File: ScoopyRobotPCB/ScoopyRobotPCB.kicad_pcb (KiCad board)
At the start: 2 copper layers, 35 parts, among them J1 18V battery, J2 Raspberry_Pi_Header, J3 Left colour sensor, J4 Right colour sensor, J5 Wheels, J6 Power, J7 Left, J8 Right, M1 Chain gearmotor, M2 Left motor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

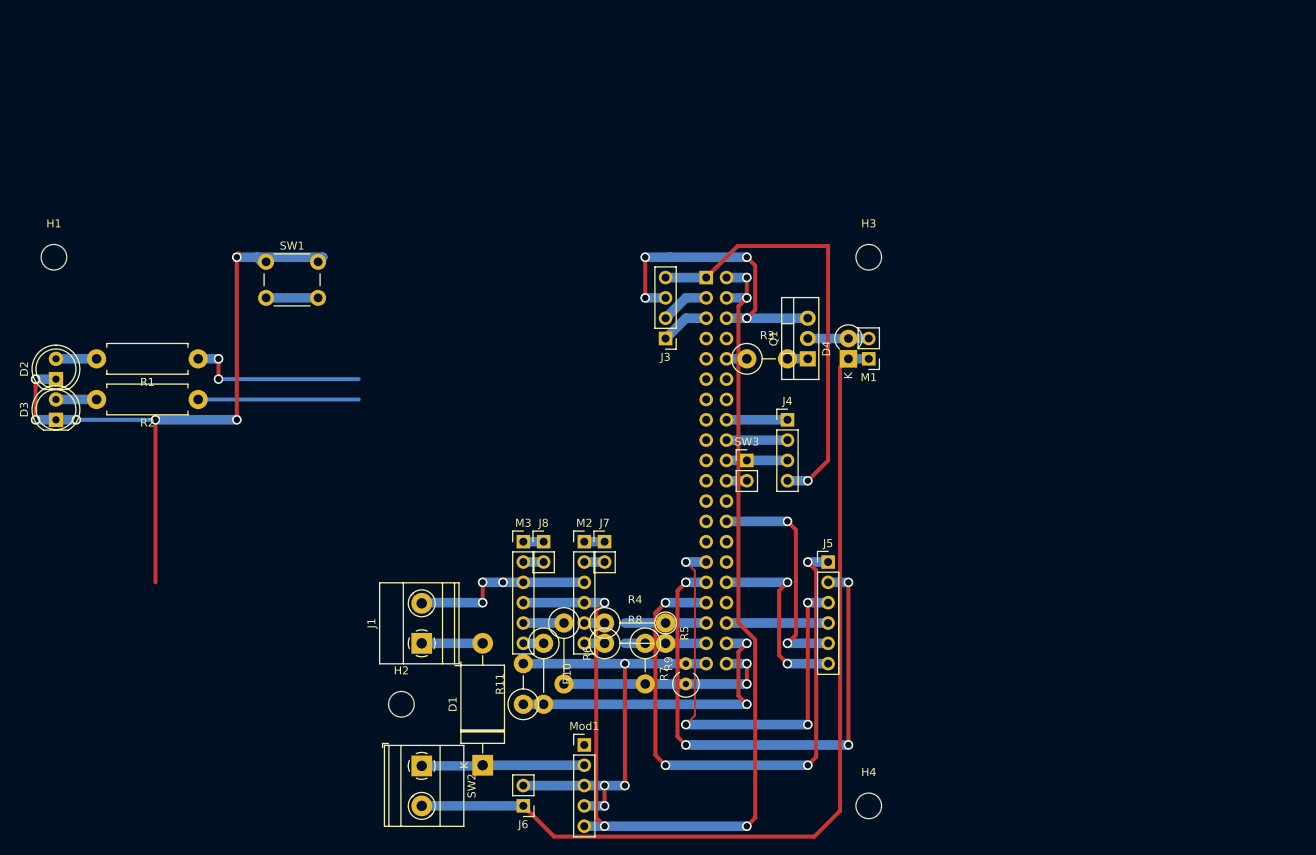
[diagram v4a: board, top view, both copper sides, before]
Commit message: Updated the PCB files to match reality
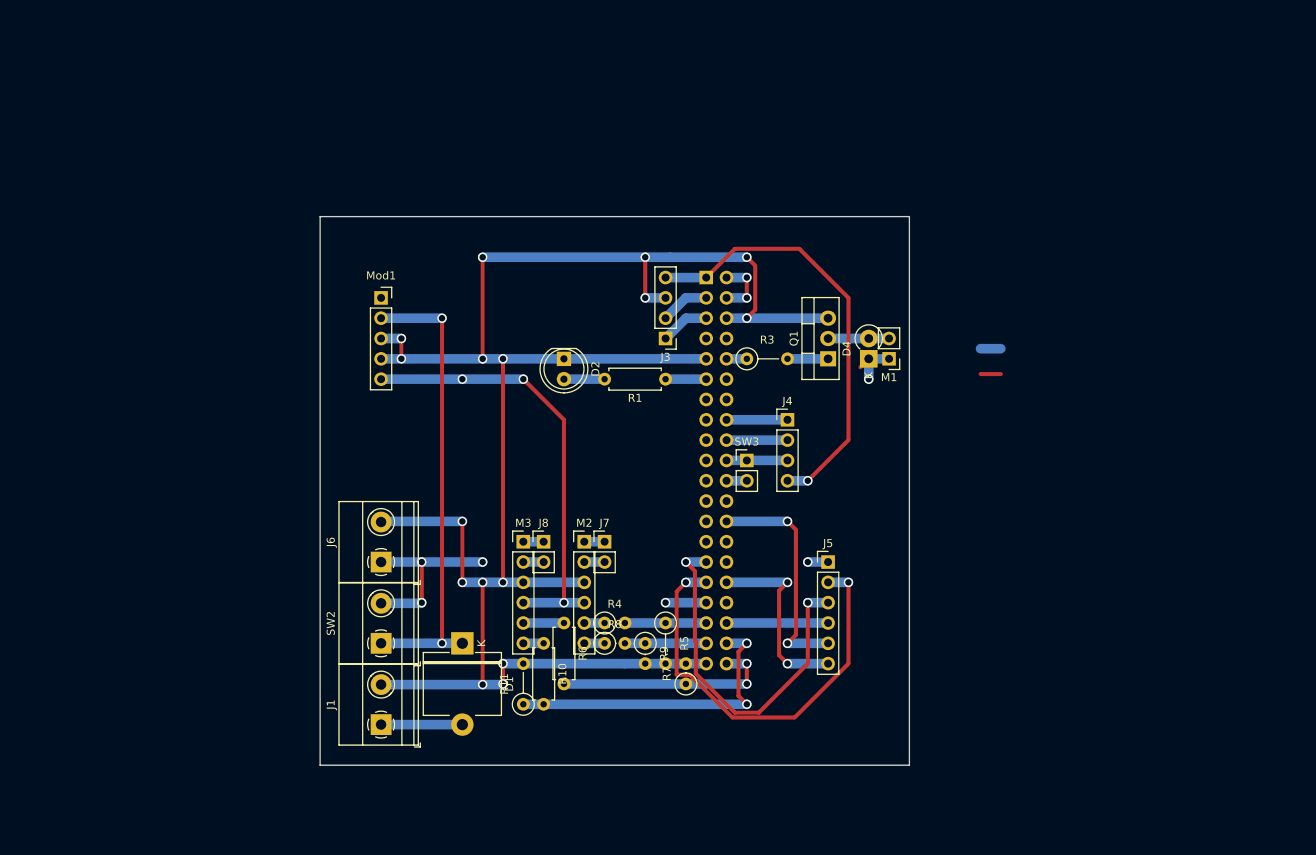
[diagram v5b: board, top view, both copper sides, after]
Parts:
- removed D3: LED, LED_THT:LED_D5.0mm
- removed H1, H2, H3, H4: MountingHole, MountingHole:MountingHole_3.2mm_M3
- removed R2: 220, Resistor_THT:R_Axial_DIN0411_L9.9mm_D3.6mm_P12.70mm_Horizontal
- removed SW1: SW_Push, Button_Switch_THT:SW_PUSH_6mm
- D1: footprint Diode_THT:D_DO-201_P15.24mm_Horizontal -> Diode_THT:D_5KP_P10.16mm_Horizontal
- J6: footprint Connector_PinHeader_2.54mm:PinHeader_1x02_P2.54mm_Vertical -> TerminalBlock_Phoenix:TerminalBlock_Phoenix_MKDS-1,5-2_1x02_P5.00mm_Horizontal
- Mod1: footprint Connector_PinHeader_2.54mm:PinHeader_1x05_P2.54mm_Vertical -> Connector_PinSocket_2.54mm:PinSocket_1x05_P2.54mm_Vertical
- Q1: value Q_NPN_Darlington_BCE -> 2SD1308
- R1: value 220 -> 150; footprint Resistor_THT:R_Axial_DIN0411_L9.9mm_D3.6mm_P12.70mm_Horizontal -> Resistor_THT:R_Axial_DIN0207_L6.3mm_D2.5mm_P7.62mm_Horizontal
- R10, R6: footprint Resistor_THT:R_Axial_DIN0411_L9.9mm_D3.6mm_P7.62mm_Vertical -> Resistor_THT:R_Axial_DIN0207_L6.3mm_D2.5mm_P7.62mm_Horizontal
- R11, R3: footprint Resistor_THT:R_Axial_DIN0411_L9.9mm_D3.6mm_P5.08mm_Vertical -> Resistor_THT:R_Axial_DIN0207_L6.3mm_D2.5mm_P5.08mm_Vertical
- R4, R8: footprint Resistor_THT:R_Axial_DIN0411_L9.9mm_D3.6mm_P7.62mm_Vertical -> Resistor_THT:R_Axial_DIN0207_L6.3mm_D2.5mm_P2.54mm_Vertical
- R5: footprint Resistor_THT:R_Axial_DIN0207_L6.3mm_D2.5mm_P2.54mm_Vertical -> Resistor_THT:R_Axial_DIN0207_L6.3mm_D2.5mm_P5.08mm_Vertical
- R7: footprint Resistor_THT:R_Axial_DIN0309_L9.0mm_D3.2mm_P2.54mm_Vertical -> Resistor_THT:R_Axial_DIN0207_L6.3mm_D2.5mm_P2.54mm_Vertical
- R9: footprint Resistor_THT:R_Axial_DIN0411_L9.9mm_D3.6mm_P5.08mm_Vertical -> Resistor_THT:R_Axial_DIN0207_L6.3mm_D2.5mm_P2.54mm_Vertical
- moved D2 63.6 mm to (109.2, 88.9), turned to -90 degrees
- moved Mod1 61.4 mm to (86.4, 81.3)
- moved R1 58.5 mm to (121.9, 91.4)
- moved J6 35.3 mm to (86.4, 114.3), turned to 90 degrees
- moved SW2 16.1 mm to (86.4, 124.5), turned to 90 degrees
- moved D1 15.5 mm to (96.5, 124.5), turned to -90 degrees
- moved J1 11.4 mm to (86.4, 134.6)
- moved M1 2.54 mm to (149.9, 88.9)
- moved Q1 2.54 mm to (142.2, 88.9)
- moved D4 2.54 mm to (147.3, 88.9)
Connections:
- J2 pad 29: unconnected-(J2-GPIO05/GCLK1-Pad29) -> /L.Mot_A
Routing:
- net +BATT: track 20.4 -> 58.4 mm, vias 0 -> 2
- net GND: track 212.6 -> 244.9 mm, vias 17 -> 16
- net /UI.LED1: track 20.1 -> 0.00 mm
- net Vdrive: track 114.7 -> 133.7 mm, vias 0 -> 4
- net +5V: track 134.7 -> 116.4 mm
- net /UI.LED0: track 22.6 -> 5.08 mm, vias 2 -> 0
- net /L.En: track 73.0 -> 59.6 mm, vias 4 -> 2
- net /L.Mot_B: track 66.9 -> 53.7 mm, vias 4 -> 2
- net /L.Mot_A: track 56.8 -> 45.7 mm, vias 4 -> 2
- net (no net): track 0.00 -> 7.62 mm
- net /UI.SW: track 6.50 -> 0.00 mm
- net Net-(D3-A): track 5.08 -> 0.00 mm
- net Net-(Q1-B): track 2.54 -> 5.08 mm
- net Net-(M3-Enc_B): track 5.08 -> 2.54 mm
- net Net-(M3-Enc_A): track 7.62 -> 5.08 mm
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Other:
- board outline added: 73.7 x 68.6 mm
- copper layers 2 -> 4
- board text added: "Insulated wires added"
- board text added: "Legend"
- board text added: "Trace on bottom layer"
- board text added: "Traces cut between holes"
- board text added: "Traces cut on a hole"
